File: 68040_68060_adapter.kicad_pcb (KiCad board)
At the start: 2 copper layers, 59.1 x 95.6 mm, 27 parts, among them IC2 74F257, IC3 MC68060RCPGA_BIG, IC4 LMS1585-3.3, U4$1 4POL, U6$1 6POL

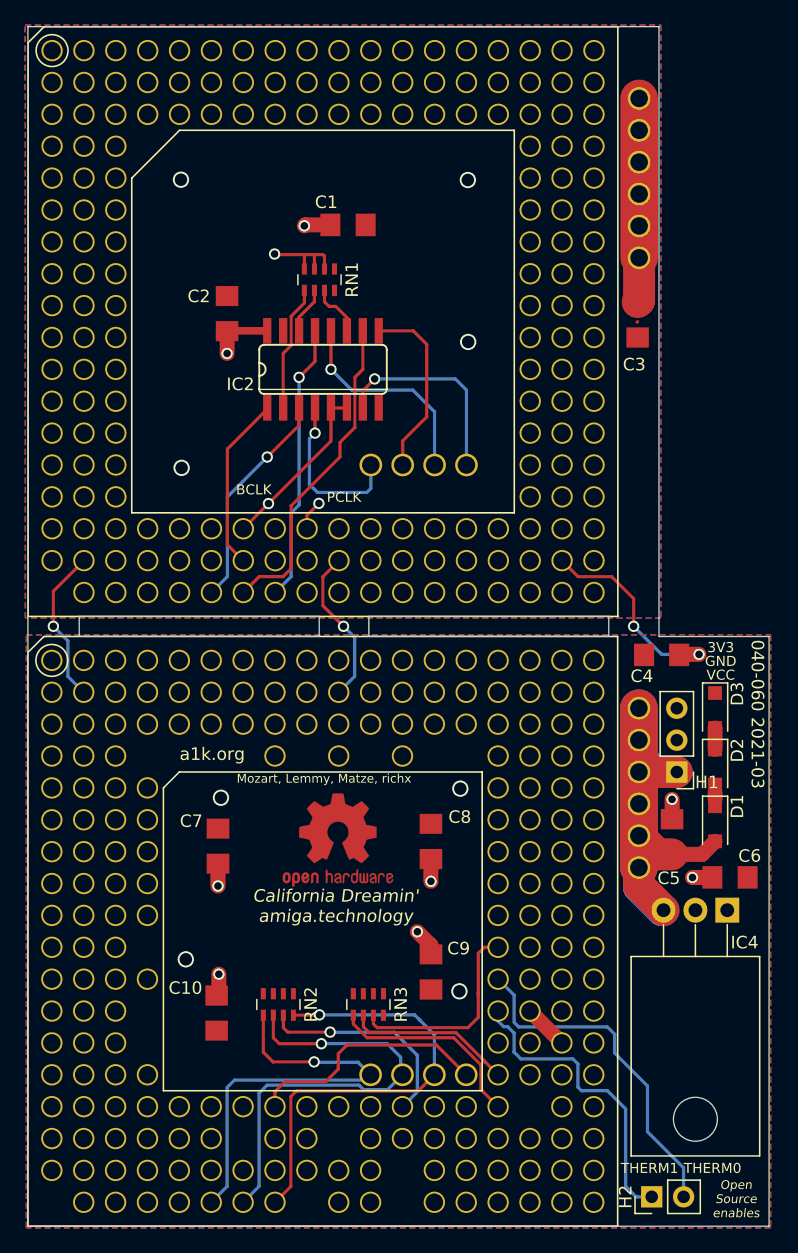
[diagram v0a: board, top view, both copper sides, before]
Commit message: Updated PCB and BOM
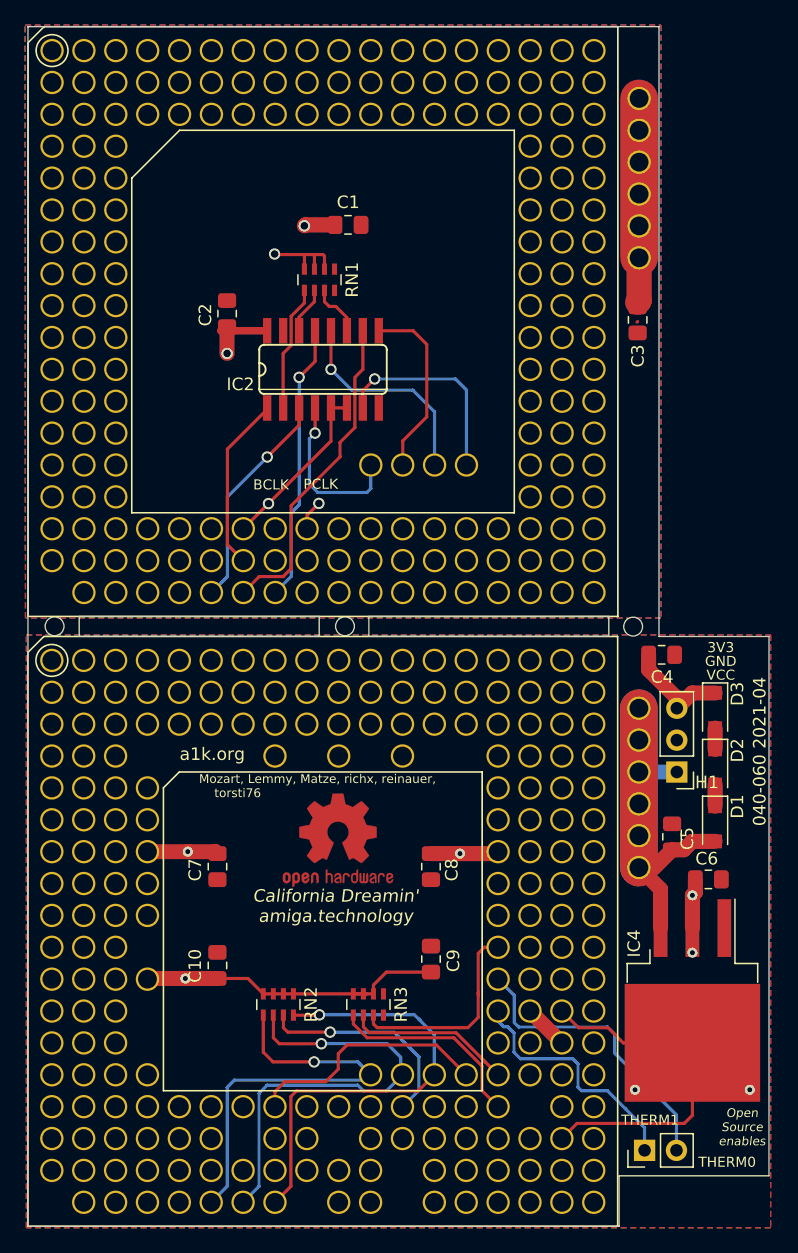
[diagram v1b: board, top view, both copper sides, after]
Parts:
- added REF**: Hole_0.5mm, MountingHole:MountingHole_2.1mm, F.Cu at (159.9, 91.4)
- added REF**: Hole_0.5mm, MountingHole:MountingHole_2.1mm, F.Cu at (136.9, 91.3)
- added REF**: Hole_0.5mm, MountingHole:MountingHole_2.1mm, F.Cu at (113.8, 91.3)
- C1, C2, C3, C4, C5, C6: footprint Bot_68040_mk2a:C1206 -> Capacitor_SMD:C_0805_2012Metric_Pad1.18x1.45mm_HandSolder
- C10, C7, C8, C9: footprint Top_68060_mk2a:C1206 -> Capacitor_SMD:C_0805_2012Metric_Pad1.18x1.45mm_HandSolder
- IC4: footprint Package_TO_SOT_THT:TO-220-3_Horizontal_TabDown -> Package_TO_SOT_SMD:TO-263-3_TabPin2
- moved IC4 7.72 mm to (164.6, 121.2), turned to 270 degrees
- moved C10 3.79 mm to (126.7, 118.4)
- moved H2 3.75 mm to (160.8, 133.1)
- moved C8 2.01 mm to (143.8, 110.5)
- moved C6 1.73 mm to (165.9, 111.5), turned to 0 degrees
- moved C7 1.63 mm to (126.7, 110.5)
- moved C9 1.02 mm to (143.8, 117.9)
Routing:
- net +3V3: track 0.00 -> 77.5 mm, vias 0 -> 7
- net GND: track 57.5 -> 4.53 mm, vias 10 -> 0
- net VCC2: track 53.9 -> 44.7 mm
- net THERM1: track 24.7 -> 20.1 mm
- net THERM0: track 27.6 -> 24.0 mm
- net ND1: track 0.52 -> 1.72 mm
- net IPL2: track 33.3 -> 34.1 mm
- net (no net): vias 8 -> 0
- added copper zone on B.Cu, net +3V3
- removed copper zone on F.Cu, net +3V3
- removed copper zone on B.Cu, net GND
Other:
- outline, holes or cut-outs redrawn
- rule pad_to_mask_clearance: 0.051 -> 0
- board text added: "040-060 2021-04"
- board text added: "Mozart, Lemmy, Matze, richx, reinauer, torsti76"
- board text removed: "040-060 2021-03"
- board text removed: "Mozart, Lemmy, Matze, richx"
